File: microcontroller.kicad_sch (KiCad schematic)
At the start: 23 parts, among them U22 W25Q128JVS, U23 RP2040, Y1 X322512MSB4SI

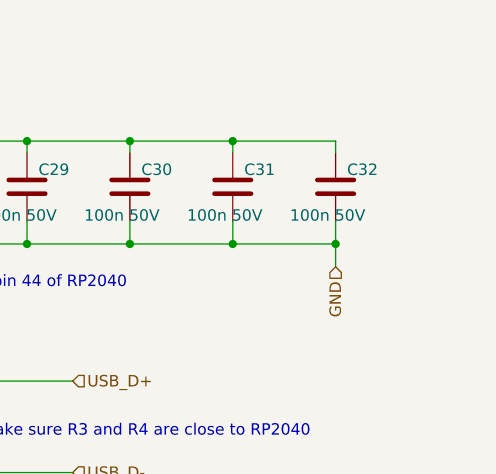
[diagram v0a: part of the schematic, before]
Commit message: Keyed stepper drivers. Larger input connector
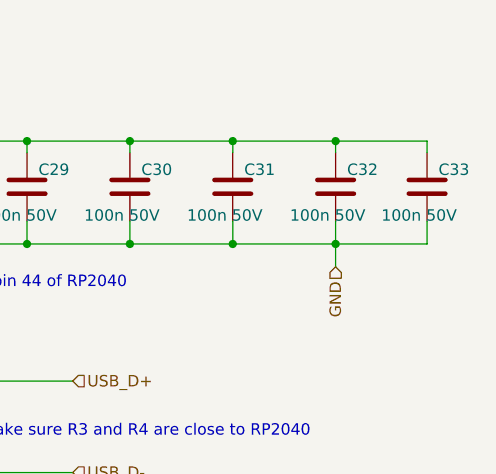
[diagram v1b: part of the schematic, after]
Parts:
- added C33: 100n 50V, Capacitor_SMD:C_0402_1005Metric, symbol Device:C
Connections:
- net GND: now also C33.2
- net VCC_3V3: now also C33.1
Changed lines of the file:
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@@
   (junction (at 220.98 27.94) (diameter 0) (color 0 0 0 0)
   )
+  (junction (at 266.7 27.94) (diameter 0) (color 0 0 0 0)
+  )
   (junction (at 143.51 21.59) (diameter 0) (color 0 0 0 0)
   )
@@
     (stroke (width 0) (type default) (color 0 0 0 0))
   )
+  (wire (pts (xy 276.86 36.83) (xy 276.86 39.37))
+    (stroke (width 0) (type default) (color 0 0 0 0))
+  )
   (wire (pts (xy 107.95 125.73) (xy 115.57 125.73))
     (stroke (width 0) (type default) (color 0 0 0 0))
@@
     (stroke (width 0) (type default) (color 0 0 0 0))
   )
+  (wire (pts (xy 266.7 27.94) (xy 276.86 27.94))
+    (stroke (width 0) (type default) (color 0 0 0 0))
+  )
   (wire (pts (xy 143.51 36.83) (xy 152.4 36.83))
     (stroke (width 0) (type default) (color 0 0 0 0))
@@
     (stroke (width 0) (type default) (color 0 0 0 0))
   )
+  (wire (pts (xy 276.86 29.21) (xy 276.86 27.94))
+    (stroke (width 0) (type default) (color 0 0 0 0))
+  )
   (wire (pts (xy 204.47 100.33) (xy 219.71 100.33))
     (stroke (width 0) (type default) (color 0 0 0 0))
@@
   )
   (wire (pts (xy 26.67 125.73) (xy 26.67 135.89))
+    (stroke (width 0) (type default) (color 0 0 0 0))
+  )
+  (wire (pts (xy 276.86 39.37) (xy 266.7 39.37))
     (stroke (width 0) (type default) (color 0 0 0 0))
   )
@@
       (effects (font (size 1.27 1.27)) hide)
     )
+    (pin "1")
+    (pin "2")
+  )
+  (symbol (lib_id "Device:C") (at 276.86 33.02 0) (unit 1)
+    (in_bom yes) (on_board yes)
+    (property "Reference" "C33" (id 0) (at 278.13 31.1149 0)
+      (effects (font (size 1.27 1.27)) (justify left))
+    )
+    (property "Value" "100n 50V" (id 1) (at 271.78 36.1949 0)
+      (effects (font (size 1.27 1.27)) (justify left))
+    )
+    (property "Footprint" "Capacitor_SMD:C_0402_1005Metric" (id 2) (at 277.8252 36.83 0)
+      (effects (font (size 1.27 1.27)) hide)
+    )
+    (property "Datasheet" "~" (id 3) (at 276.86 33.02 0)
+      (effects (font (size 1.27 1.27)) hide)
+    )
+    (property "LCSC" "C307331" (id 4) (at 276.86 33.02 0)
+      (effects (font (size 1.27 1.27)) hide)
+    )
